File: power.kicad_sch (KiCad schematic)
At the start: 31 parts, among them J4 USB_C_Receptacle_USB2.0_16P, U1 TPS62842DGRR, U2 BQ25170DSGR, U3 LM66100DCK, U6 LM66100DCK

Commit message: minor tweaks
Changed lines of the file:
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@@
 	(wire
 		(pts
-			(xy 73.66 27.94) (xy 76.2 27.94)
+			(xy 73.66 27.94) (xy 85.09 27.94)
 		)
 		(stroke
@@
 	(wire
 		(pts
+			(xy 147.32 118.11) (xy 149.86 118.11)
+		)
+		(stroke
+			(width 0)
+			(type default)
+		)
+	)
+	(wire
+		(pts
 			(xy 50.8 38.1) (xy 55.88 38.1)
 		)
@@
 	(symbol
 		(lib_id "power:Earth")
-		(at 76.2 27.94 90)
+		(at 85.09 27.94 0)
 		(unit 1)
 		(exclude_from_sim no)
@@
 		(dnp no)
 		(property "Reference" "#PWR024"
-			(at 82.55 27.94 0)
+			(at 85.09 34.29 0)
 			(effects
 				(font
@@
 		)
 		(property "Value" "GND"
-			(at 79.756 27.94 90)
+			(at 85.09 31.496 90)
 			(effects
 				(font
@@
 		)
 		(property "Footprint" ""
-			(at 76.2 27.94 0)
+			(at 85.09 27.94 0)
 			(effects
 				(font
@@
 		)
 		(property "Datasheet" "~"
-			(at 76.2 27.94 0)
+			(at 85.09 27.94 0)
 			(effects
 				(font
@@
 		)
 		(property "Description" "Power symbol creates a global label with name \"Earth\""
-			(at 76.2 27.94 0)
+			(at 85.09 27.94 0)
 			(effects
 				(font
@@
 	(symbol
 		(lib_id "power:+BATT")
-		(at 149.86 118.11 90)
+		(at 147.32 118.11 0)
 		(unit 1)
 		(exclude_from_sim no)
@@
 		(dnp no)
 		(property "Reference" "#PWR018"
-			(at 153.67 118.11 0)
+			(at 147.32 121.92 0)
 			(effects
 				(font
@@
 		)
 		(property "Value" "+BATT"
-			(at 150.114 120.396 90)
+			(at 144.526 119.888 0)
 			(effects
 				(font
@@
 		)
 		(property "Footprint" ""
-			(at 149.86 118.11 0)
+			(at 147.32 118.11 0)
 			(effects
 				(font
@@
 		)
 		(property "Datasheet" ""
-			(at 149.86 118.11 0)
+			(at 147.32 118.11 0)
 			(effects
 				(font
@@
 		)
 		(property "Description" "Power symbol creates a global label with name \"+BATT\""
-			(at 149.86 118.11 0)
+			(at 147.32 118.11 0)
 			(effects
 				(font

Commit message: updated readme, tweaked routing
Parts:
- R11: value 28.7k -> 52.3k
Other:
- note added: "R11: 0R - 1.8V, 1.74k - 2.2V, 21.5k - 3V, 28.7k - 3.1V, 38.3k - 3.2V, 52.3k - 3.3V"
- note added: "R15: 27k - 4.2V, 36k - 4.1V, 47k - 4.05V"
- note removed: "R11 – 28.7k is 3.1V, use 52.3k for 3.3V, 21.5k for 3V"
- moved on the sheet: BT1, C10, C6, C7, R10, R9, U3, U6

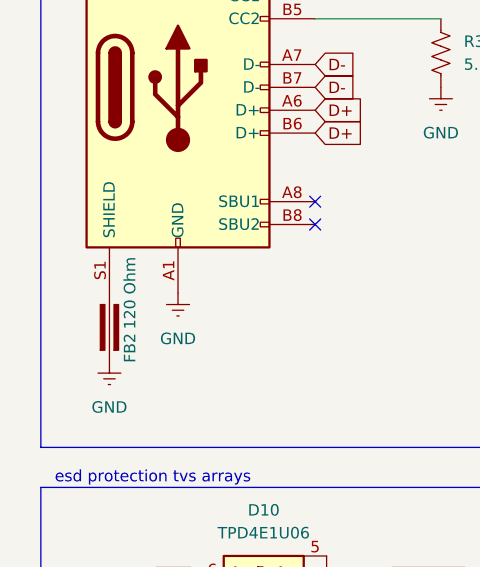
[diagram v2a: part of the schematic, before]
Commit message: trying stm32 layout
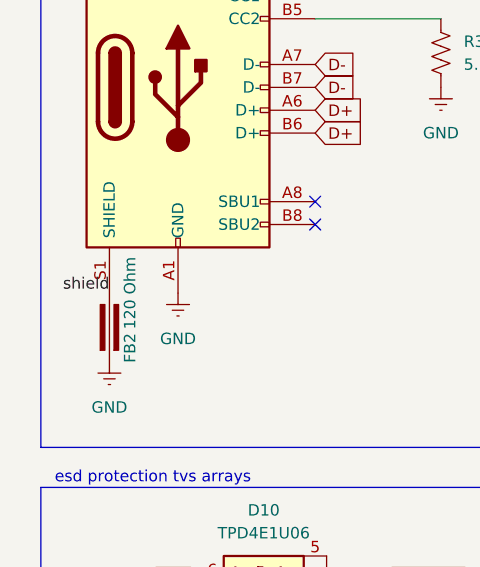
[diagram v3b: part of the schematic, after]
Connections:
- net shield: now reaches FB2.2, J4.S1 (SHIELD)
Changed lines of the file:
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@@
+		)
+	)
+	(label "shield"
+		(at 27.94 76.2 180)
+		(effects
+			(font
+				(size 1.27 1.27)
+			)
+			(justify right bottom)
 		)
 	)
